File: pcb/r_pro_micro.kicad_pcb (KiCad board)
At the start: 2 copper layers, 28 x 50 mm, 27 parts, among them J1 Conn_01x12, J2 USB_A, J3 Conn_01x12, U1 MIC5219-2.5YM5, U2 ATmega32U4-MU, Y1 16MHz

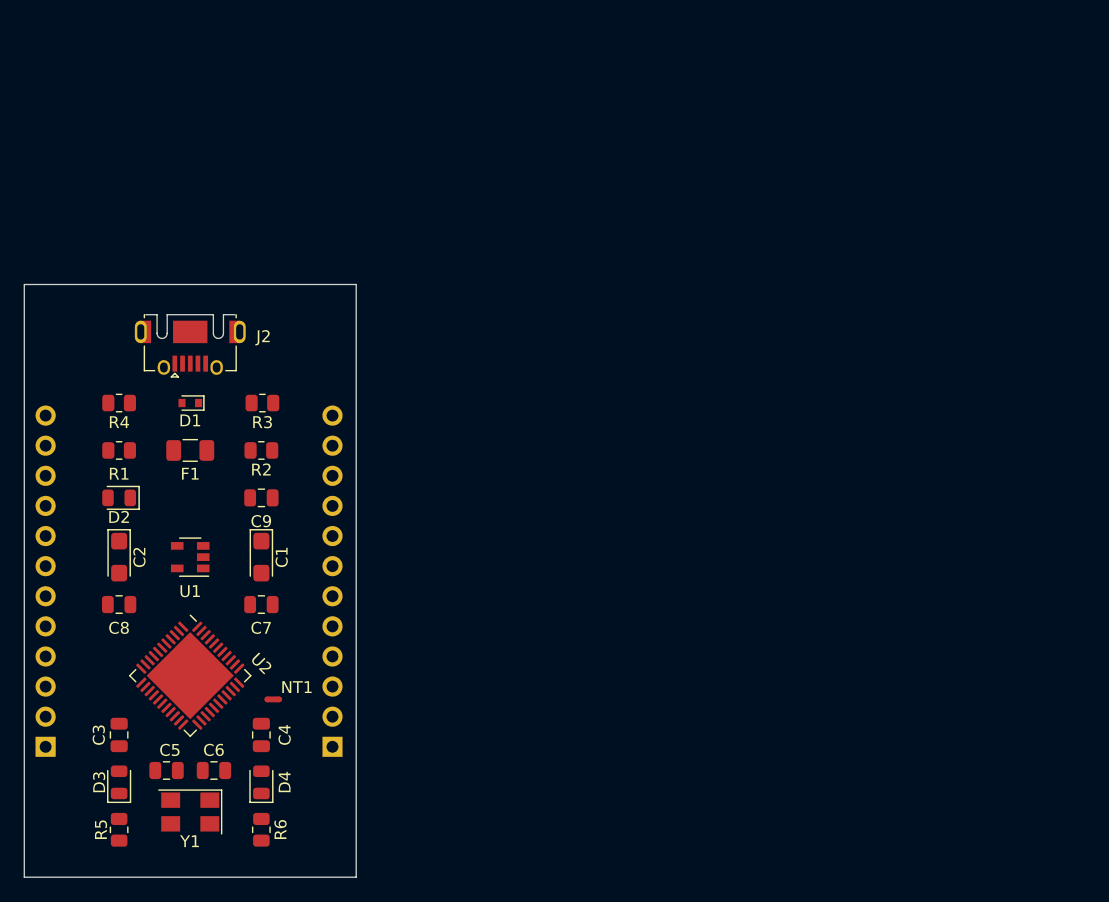
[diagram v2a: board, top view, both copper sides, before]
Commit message: ** Se hace completa el ruteo
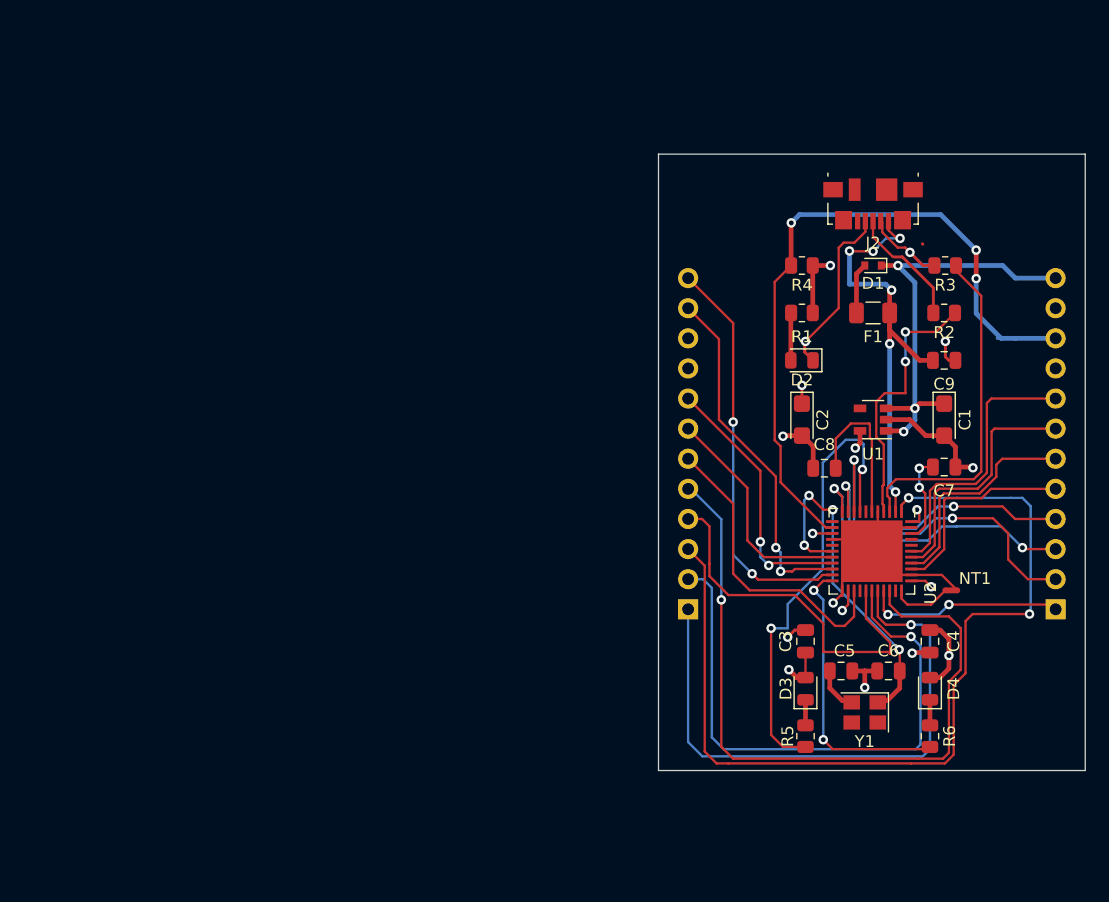
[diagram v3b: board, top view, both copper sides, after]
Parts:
- J2: footprint Connector_USB:USB_Micro-AB_Molex_47590-0001 -> Connector_USB:USB_Micro-B_Molex_47346-0001
- Y1: footprint Crystal:Crystal_SMD_5032-4Pin_5.0x3.2mm -> Crystal:Crystal_SMD_3225-4Pin_3.2x2.5mm
- moved J3 62.1 mm to (171.0, 115.4)
- moved C8 60.6 mm to (151.5, 103.5), turned to 180 degrees
- moved C1 58.8 mm to (161.6, 99.4)
- moved C2 58.8 mm to (149.6, 99.4)
- moved C7 58.8 mm to (161.6, 103.4)
- moved C9 58.8 mm to (161.6, 94.4)
- moved D1 58.8 mm to (155.6, 86.4)
- moved D2 58.8 mm to (149.6, 94.4)
- moved F1 58.8 mm to (155.6, 90.4)
- moved R1 58.8 mm to (149.6, 90.4)
- moved R2 58.8 mm to (161.6, 90.4)
- moved R3 58.8 mm to (161.7, 86.4)
- moved R4 58.8 mm to (149.6, 86.4)
- moved U1 58.8 mm to (155.6, 99.4)
- moved J2 58.6 mm to (155.6, 81.2)
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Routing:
- net /D7: track 0.00 -> 77.8 mm, vias 0 -> 2
- net GND: track 0.00 -> 64.2 mm, vias 0 -> 8
- net /D5: track 0.00 -> 62.5 mm, vias 0 -> 1
- net /RESET: track 0.00 -> 61.5 mm, vias 0 -> 3
- net /D9: track 0.00 -> 49.3 mm, vias 0 -> 1
- net /D8: track 0.00 -> 48.7 mm, vias 0 -> 1
- net Net-(R5-Pad2): track 0.00 -> 39.1 mm, vias 0 -> 2
- net VCC: track 0.00 -> 37.3 mm, vias 0 -> 6
- net /RAW: track 0.00 -> 36.7 mm, vias 0 -> 3
- net /TXO: track 0.00 -> 34.3 mm, vias 0 -> 2
- net /D6: track 0.00 -> 31.8 mm
- net /RXI: track 0.00 -> 29.9 mm, vias 0 -> 2
- net Net-(R3-Pad1): track 0.00 -> 28.9 mm
- net Net-(C6-Pad1): track 0.00 -> 28.6 mm, vias 0 -> 4
- net /SCK: track 0.00 -> 28.0 mm, vias 0 -> 2
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- added copper zone on In2.Cu.3V3, net +3V3
- added copper zone on In1.Cu.GND, net GND
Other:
- board size 28 x 50 mm -> 36 x 52 mm
- copper layers 2 -> 4
- net class Default: trace_width 0.25 -> 0.2

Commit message: Se reahace PCB
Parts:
- removed NT1: Net-Tie_2, NetTie:NetTie-2_SMD_Pad0.5mm
- added FID1: Fiducial, Fiducial:Fiducial_0.5mm_Mask1mm, F.Cu at (111.0, 71.0)
- added FID2: Fiducial, Fiducial:Fiducial_0.5mm_Mask1mm, B.Cu at (139.0, 114.0)
- added H1: MountingHole, MountingHole:MountingHole_2.1mm, F.Cu at (137.5, 72.5)
- added H2: MountingHole, MountingHole:MountingHole_2.1mm, F.Cu at (112.5, 112.5)
- J1, J3: moved to F.Cu
- moved J3 49.1 mm to (138.0, 79.0)
- moved J1 45.9 mm to (112.0, 79.0)
- moved R5 33.9 mm to (118.8, 112.8), turned to 180 degrees
- moved C7 33.4 mm to (129.5, 94.0)
- moved D3 33.3 mm to (118.8, 110.2), turned to 180 degrees
- moved C3 32.8 mm to (118.8, 107.8), turned to 0 degrees
- moved C1 32.6 mm to (130.5, 89.5)
- moved U2 32.5 mm to (125.0, 99.2), turned to 315 degrees
- moved C8 32.4 mm to (120.5, 94.0)
- moved C9 32.3 mm to (130.5, 85.5)
- moved U1 32.3 mm to (125.0, 89.0)
- moved R2 32.2 mm to (130.5, 82.0)
- moved R3 32.2 mm to (130.5, 78.5)
- moved Y1 32.1 mm to (125.2, 111.8)
- moved C5 31.9 mm to (123.2, 108.8), turned to 180 degrees
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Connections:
- J1 pad 1: /D9 -> /TXO
- J1 pad 10: GND -> /D7
- J1 pad 11: /RXI -> /D8
- J1 pad 12: /TXO -> /D9
- J1 pad 2: /D8 -> /RXI
- J1 pad 3: /D7 -> GND
- J1 pad 4: /D6 -> GND
- J1 pad 5: /D5 -> /D2
- J1 pad 6: /D4 -> /D3
- J1 pad 7: /D3 -> /D4
- J1 pad 8: /D2 -> /D5
- J1 pad 9: GND -> /D6
- J3 pad 1: /D10 -> /RAW
- J3 pad 10: /RESET -> /MISO
- J3 pad 11: GND -> /MOSI
- J3 pad 12: /RAW -> /D10
- J3 pad 2: /MOSI -> GND
- J3 pad 3: /MISO -> /RESET
- J3 pad 4: /SCK -> +3V3
- J3 pad 5: /A0 -> /A3
- J3 pad 6: /A1 -> /A2
- J3 pad 7: /A2 -> /A1
- J3 pad 8: /A3 -> /A0
- J3 pad 9: +3V3 -> /SCK
- U2 pad 33: Net-(NT1-Pad1) -> GND
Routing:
- net /D7: track 77.8 -> 18.0 mm
- net /D5: track 62.5 -> 27.4 mm, vias 1 -> 4
- net /RXI: track 29.9 -> 61.7 mm
- net /MISO: track 25.3 -> 52.0 mm
- net /MOSI: track 27.2 -> 53.8 mm
- net /D2: track 22.3 -> 48.7 mm, vias 2 -> 3
- net /TXO: track 34.3 -> 59.0 mm
- net /D3: track 19.3 -> 43.2 mm, vias 0 -> 3
- net /D6: track 31.8 -> 54.3 mm, vias 0 -> 1
- net /SCK: track 28.0 -> 47.5 mm
- net +3V3: track 25.9 -> 42.9 mm, vias 9 -> 6
- net GND: track 64.2 -> 77.5 mm, vias 8 -> 9
- net Net-(R5-Pad2): track 39.1 -> 27.9 mm, vias 2 -> 0
- net Net-(C5-Pad1): track 3.33 -> 14.3 mm, vias 0 -> 2
- net Net-(C8-Pad1): track 13.4 -> 4.01 mm
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- added copper zone on F.Cu, net +3V3
- added copper zone on B.Cu, net GND
- removed copper zone on In2.Cu.3V3, net +3V3
- removed copper zone on In1.Cu.GND, net GND
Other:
- board size 36 x 52 mm -> 30 x 45 mm
- copper layers 4 -> 2
- board text added: "10"
- board text added: "14"
- board text added: "15"
- board text added: "16"
- board text added: "2"
- board text added: "3"
- board text added: "4"
- board text added: "5"
- board text added: "6"
- board text added: "7"
- board text added: "8"
- board text added: "9"
- board text added: "A0"
- board text added: "A1"
- board text added: "A2"
- board text added: "A3"
- board text added: "GND"
- board text added: "RAW"
- board text added: "RST"
- board text added: "RXI"
- board text added: "TXO"
- board text added: "VCC"

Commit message: Se agrega notas en PCB
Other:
- board text added: "* Las restricciones para el ancho de las pistas son los utilizados por fabricantes de industria nacional. * Se utiliza las capacidades de fabricacion nacional (Mayer). * Las capacidad de mayer planteada para este modulo fue de 8 mils. * La grilla utilizada para acomodar los componentes como primera aproximacion fue de 1mm. * La grilla utilizada para routear las pistas fue de 0.2mm."
- board text added: "Replica pro micro Sparkfun Oct - 2020 DISEÑADO EN ARG."
